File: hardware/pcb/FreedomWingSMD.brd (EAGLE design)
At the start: 63.2 x 33 mm, 23 parts

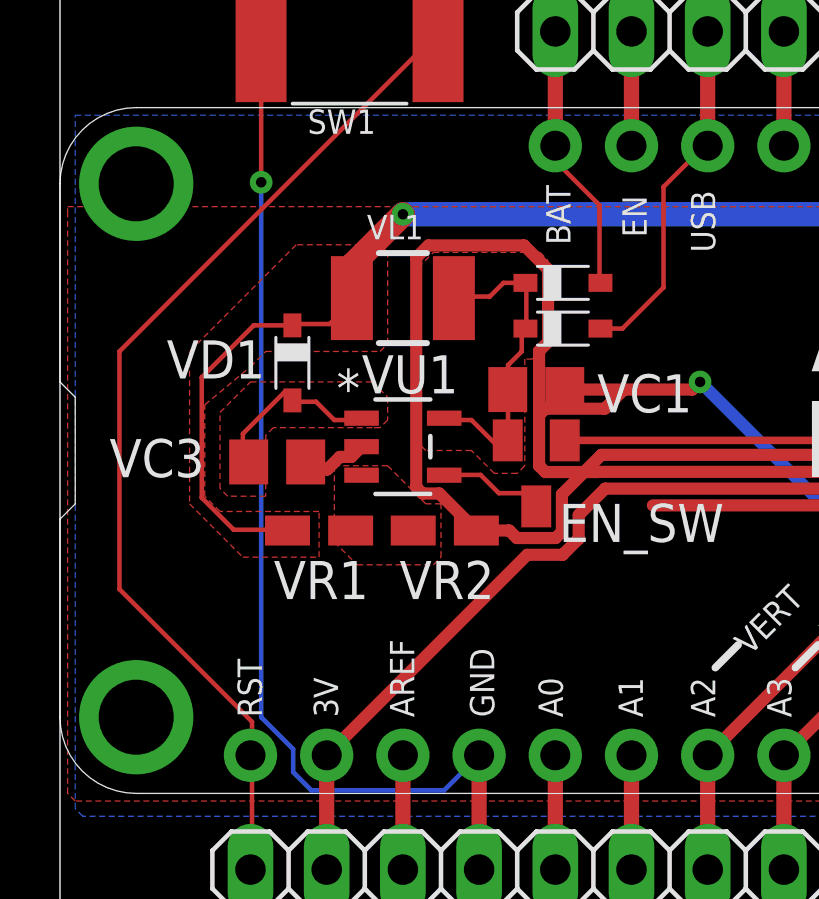
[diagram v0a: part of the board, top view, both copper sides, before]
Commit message: Fixed schematic issues w/Voltage Regulator
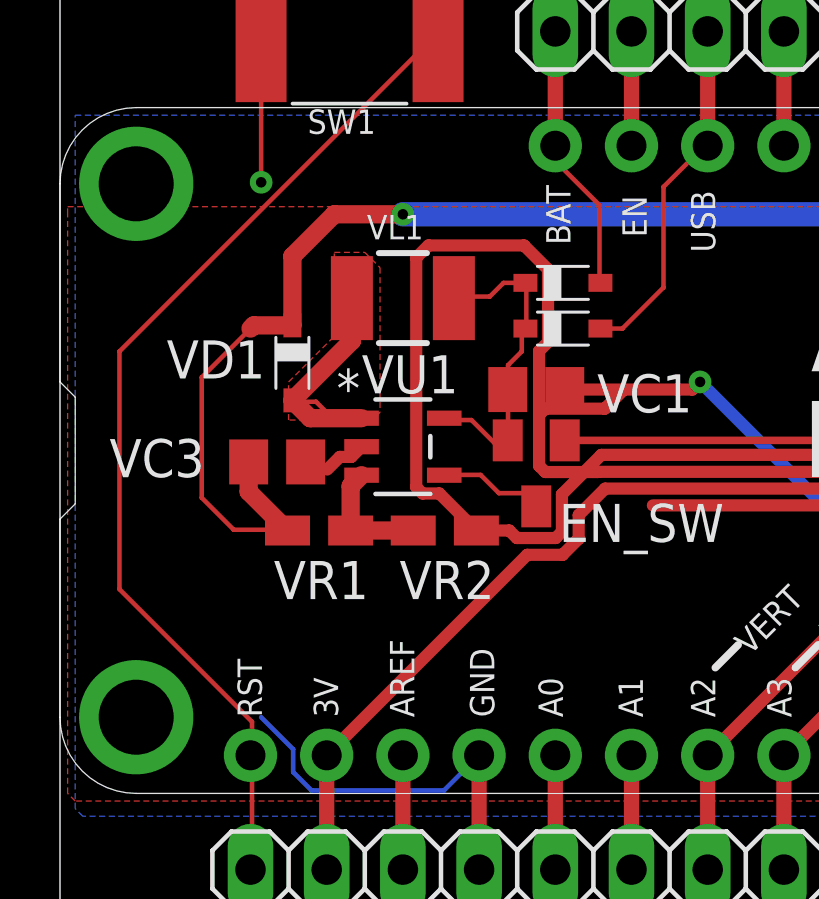
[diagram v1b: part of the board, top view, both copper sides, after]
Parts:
- VC3: value (none) -> 2.2nF
- VR1: value (none) -> 240K
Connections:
- net N$26: now also VL1.2; no longer VC3.2
- net V12: now also VC3.2; no longer VL1.2
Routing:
- net GND: track 222.5 -> 203.9 mm
- net N$8: track 0.00 -> 4.08 mm
- net V12: track 75.2 -> 78.7 mm
- net N$26: track 6.31 -> 9.43 mm
- removed copper zone on layer 1, net N$8
- removed copper zone on layer 1, net V12
- removed copper zone on layer 1, net VMAX
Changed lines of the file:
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@@
 <drawing>
 <settings>
-<setting alwaysvectorfont="yes"/>
+<setting alwaysvectorfont="no"/>
 <setting verticaltext="up"/>
 </settings>
@@
 <attribute name="VALUE" x="13.13" y="24.19" size="0.8128" layer="27" rot="R180"/>
 </element>
-<element name="VC3" library="rcl" library_urn="urn:adsk.eagle:library:334" package="C0805" package3d_urn="urn:adsk.eagle:package:23617/2" value="" x="7.239" y="16.129" smashed="yes" rot="R180">
+<element name="VC3" library="rcl" library_urn="urn:adsk.eagle:library:334" package="C0805" package3d_urn="urn:adsk.eagle:package:23617/2" value="2.2nF" x="7.239" y="16.129" smashed="yes" rot="R180">
 <attribute name="NAME" x="1.651" y="15.621" size="1.27" layer="25"/>
 <attribute name="POPULARITY" value="88" x="7.239" y="16.129" size="1.778" layer="27" rot="R180" display="off"/>
@@
 <attribute name="VALUE" x="13.462" y="16.383" size="1.27" layer="27" rot="R180"/>
 </element>
-<element name="VR1" library="rcl" library_urn="urn:adsk.eagle:library:334" package="R0805W" package3d_urn="urn:adsk.eagle:package:23537/2" value="" x="8.636" y="13.843" smashed="yes" rot="R180">
+<element name="VR1" library="rcl" library_urn="urn:adsk.eagle:library:334" package="R0805W" package3d_urn="urn:adsk.eagle:package:23537/2" value="240K" x="8.636" y="13.843" smashed="yes" rot="R180">
 <attribute name="NAME" x="10.287" y="12.827" size="1.27" layer="25" rot="R180"/>
 <attribute name="POPULARITY" value="3" x="8.636" y="13.843" size="1.778" layer="27" rot="R180" display="off"/>
@@
 <contactref element="VU1" pad="2"/>
 <contactref element="VC1" pad="2"/>
-<contactref element="VC3" pad="1"/>
 <contactref element="VR2" pad="1"/>
 <contactref element="SW1" pad="P$2"/>
 <wire x1="6.7056" y1="25.4508" x2="6.7056" y2="29.8704" width="0.1524" layer="1"/>
 <wire x1="6.7056" y1="29.8704" x2="6.702" y2="29.972" width="0.1524" layer="1"/>
-<wire x1="6.7056" y1="7.62" x2="6.7056" y2="25.4508" width="0.1524" layer="16"/>
 <wire x1="7.7724" y1="6.5532" x2="6.7056" y2="7.62" width="0.1524" layer="16"/>
 <wire x1="7.7724" y1="5.7912" x2="7.7724" y2="6.5532" width="0.1524" layer="16"/>
@@
 <wire x1="6.7056" y1="25.4508" x2="6.7056" y2="25.4" width="0.1524" layer="1"/>
 <via x="6.7056" y="25.4508" extent="1-16" drill="0.35"/>
-<polygon width="0.254" layer="1" rank="2">
+<polygon width="0.254" layer="1" rank="3">
 <vertex x="0.254" y="24.638"/>
 <vertex x="52.578" y="24.638"/>
@@
 <wire x1="10.05205" y1="16.637" x2="9.71165" y2="16.2966" width="0.4064" layer="1"/>
 <wire x1="9.71165" y1="16.2966" x2="9.32690625" y2="16.2966" width="0.4064" layer="1"/>
-<wire x1="8.90530625" y1="15.875" x2="8.189" y2="16.129" width="0.4064" layer="1"/>
 <wire x1="9.32690625" y1="16.2966" x2="8.90530625" y2="15.875" width="0.4064" layer="1"/>
 <wire x1="12.08280625" y1="15.0774" x2="11.8745" y2="15.28570625" width="0.4064" layer="1"/>
@@
 <wire x1="40.9884" y1="13.8756" x2="40.9884" y2="11.85270625" width="0.4064" layer="1"/>
 <wire x1="40.9884" y1="11.85270625" x2="41.894" y2="10.94710625" width="0.4064" layer="1"/>
+<contactref element="VC3" pad="1"/>
 </signal>
 <signal name="USB">
@@
 <contactref element="J2" pad="7"/>
 <contactref element="J2" pad="9"/>
-<contactref element="VD1" pad="C"/>
-<contactref element="VL1" pad="2"/>
 <contactref element="VR1" pad="2"/>
 <wire x1="58.8264" y1="16.3068" x2="58.8264" y2="15.24" width="0.1524" layer="16"/>
@@
 <wire x1="58.8264" y1="15.24" x2="58.697" y2="15.13" width="0.1524" layer="16"/>
 <wire x1="58.8264" y1="20.574" x2="58.697" y2="20.66" width="0.1524" layer="16"/>
-<wire x1="8.9916" y1="20.7264" x2="7.7724" y2="20.7264" width="0.1524" layer="1"/>
-<wire x1="9.7536" y1="21.4884" x2="8.9916" y2="20.7264" width="0.1524" layer="1"/>
-<wire x1="7.7724" y1="20.7264" x2="7.747" y2="20.681" width="0.1524" layer="1"/>
-<wire x1="9.7536" y1="21.4884" x2="9.73" y2="21.59" width="0.1524" layer="1"/>
 <wire x1="5.7912" y1="13.8684" x2="7.7724" y2="13.8684" width="0.1524" layer="1"/>
 <wire x1="4.7244" y1="14.9352" x2="5.7912" y2="13.8684" width="0.1524" layer="1"/>
 <wire x1="4.7244" y1="18.9484" x2="4.7244" y2="14.9352" width="0.1524" layer="1"/>
-<wire x1="7.747" y1="20.681" x2="6.457" y2="20.681" width="0.1524" layer="1"/>
-<wire x1="6.457" y1="20.681" x2="4.7244" y2="18.9484" width="0.1524" layer="1"/>
+<wire x1="6.35" y1="20.574" x2="4.7244" y2="18.9484" width="0.1524" layer="1"/>
 <wire x1="7.7724" y1="13.8684" x2="7.5835" y2="13.843" width="0.1524" layer="1"/>
-<polygon width="0.1524" layer="1">
-<vertex x="10.668" y="19.812"/>
-<vertex x="10.922" y="20.066"/>
-<vertex x="10.922" y="23.114"/>
-<vertex x="10.668" y="23.368"/>
-<vertex x="7.874" y="23.368"/>
-<vertex x="4.318" y="19.812"/>
-<vertex x="4.318" y="14.732"/>
-<vertex x="6.096" y="12.954"/>
-<vertex x="8.636" y="12.954"/>
-<vertex x="8.636" y="14.478"/>
-<vertex x="5.334" y="14.478"/>
-<vertex x="4.826" y="14.986"/>
-<vertex x="4.826" y="18.034"/>
-<vertex x="6.35" y="19.304"/>
-<vertex x="6.858" y="19.812"/>
-</polygon>
-<wire x1="9.73" y1="21.59" x2="9.73" y2="22.684" width="0.8128" layer="1"/>
-<wire x1="9.73" y1="22.684" x2="11.43" y2="24.384" width="0.8128" layer="1"/>
 <via x="11.43" y="24.384" extent="1-16" drill="0.35"/>
 <wire x1="37.8685375" y1="22.5552" x2="40.8714625" y2="22.5552" width="0.8128" layer="16"/>
@@
 <wire x1="58.720690625" y1="20.644253125" x2="58.712746875" y2="20.644253125" width="0.8128" layer="16"/>
 <wire x1="58.712746875" y1="20.644253125" x2="58.697" y2="20.66" width="0.8128" layer="16"/>
+<contactref element="VD1" pad="C"/>
+<contactref element="VC3" pad="2"/>
+<wire x1="7.5835" y1="13.843" x2="6.289" y2="15.1375" width="0.6096" layer="1"/>
+<wire x1="6.289" y1="15.1375" x2="6.289" y2="16.129" width="0.6096" layer="1"/>
+<wire x1="6.35" y1="20.574" x2="6.457" y2="20.681" width="0.6096" layer="1"/>
+<wire x1="6.457" y1="20.681" x2="7.747" y2="20.681" width="0.6096" layer="1"/>
+<wire x1="7.747" y1="20.681" x2="7.747" y2="22.987" width="0.6096" layer="1"/>
+<wire x1="9.144" y1="24.384" x2="11.43" y2="24.384" width="0.6096" layer="1"/>
+<wire x1="7.747" y1="22.987" x2="9.144" y2="24.384" width="0.6096" layer="1"/>
 </signal>
 <signal name="N$17">
@@
 <wire x1="15.514" y1="22.098" x2="14.7828" y2="22.098" width="0.1524" layer="1"/>
 <wire x1="13.2588" y1="21.6408" x2="13.13" y2="21.59" width="0.1524" layer="1"/>
-<polygon width="0.1524" layer="1" isolate="0.254">
-<vertex x="12.446" y="23.114"/>
-<vertex x="16.002" y="23.114"/>
-<vertex x="16.256" y="22.86"/>
-<vertex x="16.256" y="20.066"/>
-<vertex x="16.002" y="19.812"/>
-<vertex x="15.748" y="19.558"/>
-<vertex x="15.494" y="19.558"/>
-<vertex x="15.494" y="16.002"/>
-<vertex x="15.24" y="15.748"/>
-<vertex x="14.478" y="15.748"/>
-<vertex x="13.716" y="16.51"/>
-<vertex x="12.192" y="16.51"/>
-<vertex x="11.938" y="16.764"/>
-<vertex x="11.938" y="22.606"/>
-</polygon>
 </signal>
 <signal name="N$26">
 <contactref element="VU1" pad="1"/>
-<contactref element="VD1" pad="A"/>
-<contactref element="VC3" pad="2"/>
 <wire x1="8.5344" y1="18.1356" x2="7.7724" y2="18.1356" width="0.1524" layer="1"/>
 <wire x1="9.144" y1="17.526" x2="8.5344" y2="18.1356" width="0.1524" layer="1"/>
 <wire x1="9.906" y1="17.526" x2="9.144" y2="17.526" width="0.1524" layer="1"/>
-<wire x1="7.7724" y1="18.1356" x2="7.747" y2="18.181" width="0.1524" layer="1"/>
 <wire x1="9.906" y1="17.526" x2="10.05205" y2="17.587" width="0.1524" layer="1"/>
-<wire x1="6.096" y1="17.0688" x2="6.096" y2="16.002" width="0.1524" layer="1"/>
-<wire x1="7.4676" y1="18.4404" x2="6.096" y2="17.0688" width="0.1524" layer="1"/>
-<wire x1="7.62" y1="18.4404" x2="7.4676" y2="18.4404" width="0.1524" layer="1"/>
-<wire x1="7.7724" y1="18.288" x2="7.62" y2="18.4404" width="0.1524" layer="1"/>
-<wire x1="6.096" y1="16.002" x2="6.289" y2="16.129" width="0.1524" layer="1"/>
-<wire x1="7.7724" y1="18.288" x2="7.747" y2="18.181" width="0.1524" layer="1"/>
-<polygon width="0.1524" layer="1">
-<vertex x="6.858" y="14.986"/>
-<vertex x="5.588" y="14.986"/>
-<vertex x="5.334" y="15.24"/>
-<vertex x="5.334" y="17.78"/>
-<vertex x="6.35" y="18.796"/>
-<vertex x="10.414" y="18.796"/>
-<vertex x="10.922" y="18.288"/>
-<vertex x="10.922" y="17.526"/>
-<vertex x="10.668" y="17.272"/>
-<vertex x="10.414" y="17.272"/>
-<vertex x="7.112" y="17.272"/>
-<vertex x="6.858" y="17.018"/>
+<contactref element="VD1" pad="A"/>
+<contactref element="VL1" pad="2"/>
+<wire x1="9.7536" y1="21.4884" x2="9.73" y2="21.59" width="0.1524" layer="1"/>
+<wire x1="7.747" y1="18.181" x2="9.73" y2="20.164" width="0.6096" layer="1"/>
+<wire x1="9.73" y1="20.164" x2="9.73" y2="21.59" width="0.6096" layer="1"/>
+<wire x1="10.05205" y1="17.587" x2="8.341" y2="17.587" width="0.6096" layer="1"/>
+<wire x1="8.341" y1="17.587" x2="7.747" y2="18.181" width="0.6096" layer="1"/>
+<polygon width="0.1524" layer="1" rank="2">
+<vertex x="9.144" y="23.114"/>
+<vertex x="10.16" y="23.114"/>
+<vertex x="10.668" y="22.606"/>
+<vertex x="10.668" y="17.78"/>
+<vertex x="10.414" y="17.526"/>
+<vertex x="7.62" y="17.526"/>
+<vertex x="7.62" y="18.796"/>
+<vertex x="9.144" y="20.32"/>
 </polygon>
 </signal>
 <signal name="N$8">
 <contactref element="VU1" pad="3"/>
-<polygon width="0.1524" layer="1">
-<vertex x="10.922" y="16.002"/>
-<vertex x="9.144" y="16.002"/>
-<vertex x="9.144" y="13.462"/>
-<vertex x="9.906" y="12.7"/>
-<vertex x="12.446" y="12.7"/>
-<vertex x="12.7" y="12.954"/>
-<vertex x="12.7" y="14.732"/>
-<vertex x="12.192" y="14.732"/>
-</polygon>
 <contactref element="VR2" pad="2"/>
 <contactref element="VR1" pad="1"/>
+<wire x1="11.7745" y1="13.843" x2="9.6885" y2="13.843" width="0.6096" layer="1"/>
+<wire x1="9.6885" y1="13.843" x2="9.6885" y2="15.32345" width="0.6096" layer="1"/>
+<wire x1="9.6885" y1="15.32345" x2="10.05205" y2="15.687" width="0.6096" layer="1"/>
 </signal>
 <signal name="N$25">

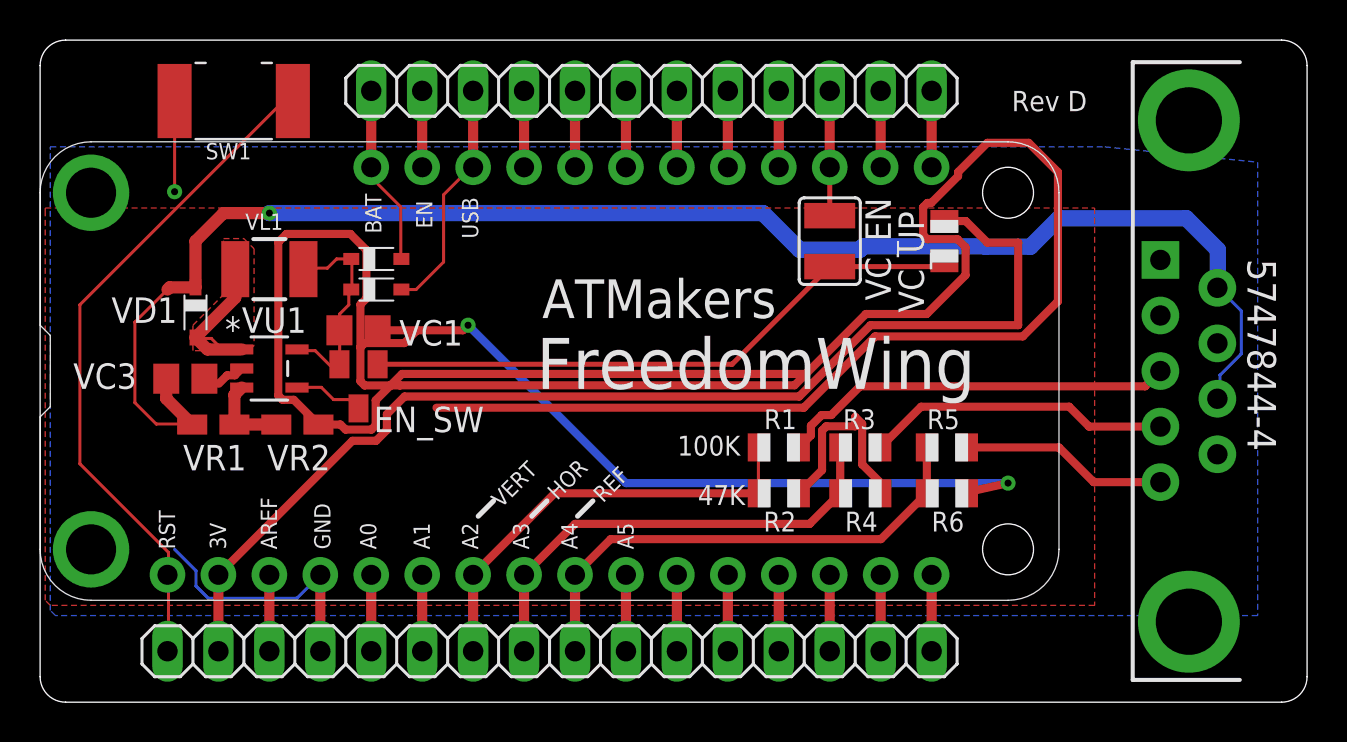
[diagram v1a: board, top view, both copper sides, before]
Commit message: Added values and tweaked for 12V
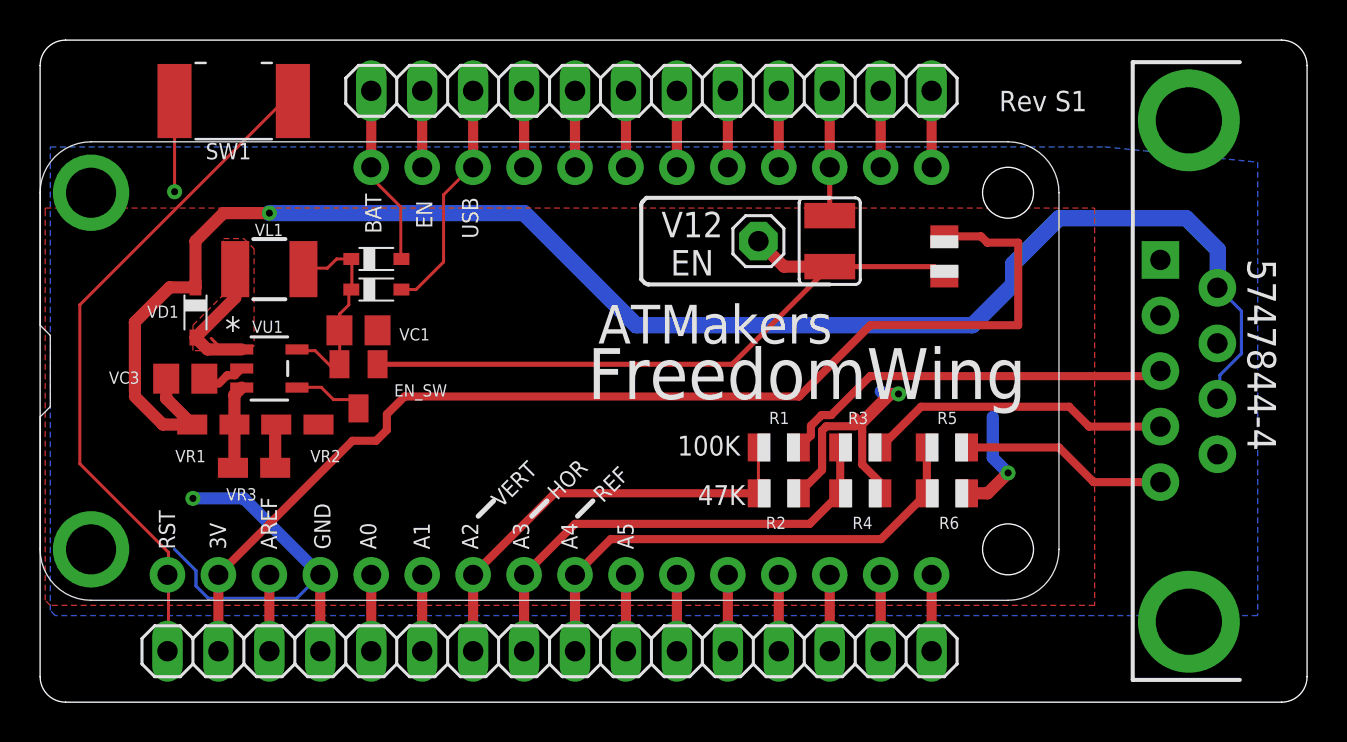
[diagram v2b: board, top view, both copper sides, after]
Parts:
- added VC_ENPIN: (no value), adafruit:1X01
- added VR3: 680, rcl:R0805W
- VC1: value (none) -> 10mF
- VC3: value 2.2nF -> 2.2mF
- VL1: value (none) -> 10mH
- VR2: value (none) -> 27K
- moved VC_UP 0.76 mm to (45.1, 22.2)
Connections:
- new net N$31: VR2.2, VR3.1
- net N$28: now also VC_ENPIN.1
- net N$8: now also VR3.2; no longer VR2.2
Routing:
- net GND: track 203.9 -> 46.1 mm, vias 3 -> 4
- net N$28: track 30.4 -> 34.6 mm
- net V12: track 78.7 -> 81.8 mm
- net N$31: track 0.00 -> 2.18 mm
- net N$26: track 9.43 -> 8.67 mm
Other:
- board text added: "Rev S1"
- board text added: "V12 EN"
- board text removed: "Rev D"
- board text removed: "w/AbleGamers & GRA-V"

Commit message: Switched to 2 layers & added stuff
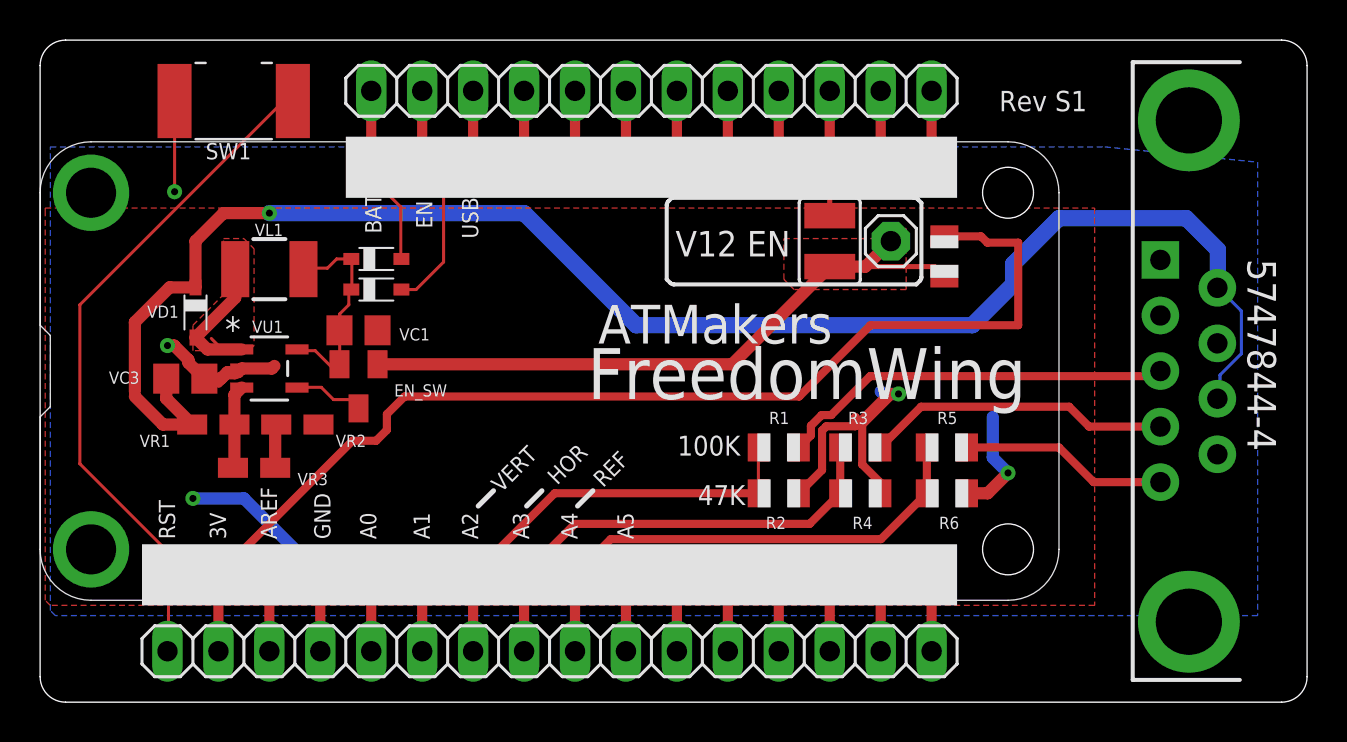
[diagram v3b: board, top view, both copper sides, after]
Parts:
- moved VC_ENPIN 6.60 mm to (42.4, 23.0)
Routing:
- net GND: track 46.1 -> 52.5 mm, vias 4 -> 5
- net N$28: track 34.6 -> 34.1 mm
- added copper zone on layer 1, net N$28
